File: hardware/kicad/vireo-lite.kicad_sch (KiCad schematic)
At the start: 0 parts

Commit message: usb interface
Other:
- removed sheet Analog Front End (AFE)
- sheet Inputs ports: added PHANTOM_48V; removed none
- sheet USB Interface ports: added USB_N, USB_P, VBUS_RAW; removed none
- sheet User Interface ports: added HIZ_FET_GATE; removed none

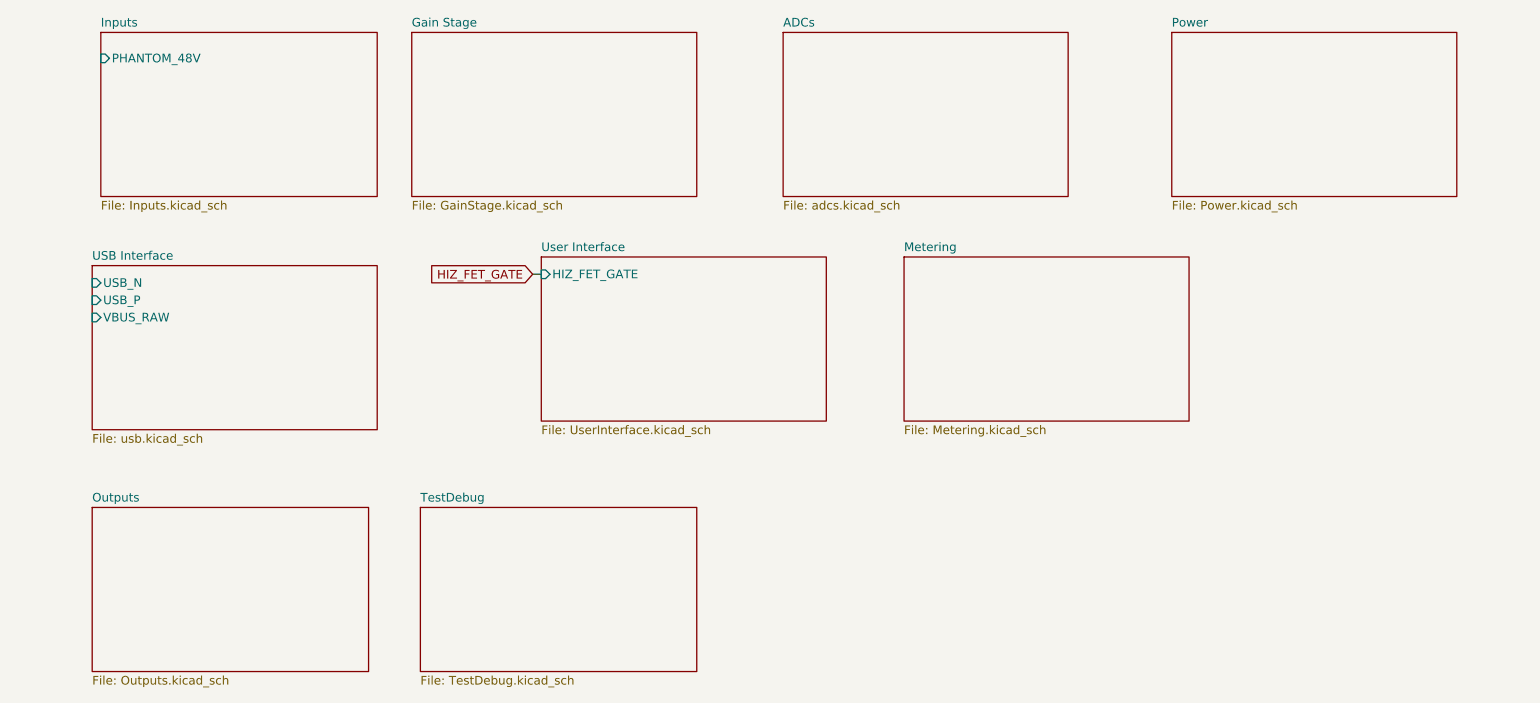
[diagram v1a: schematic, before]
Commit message: add phtm indicator and mcu sheet
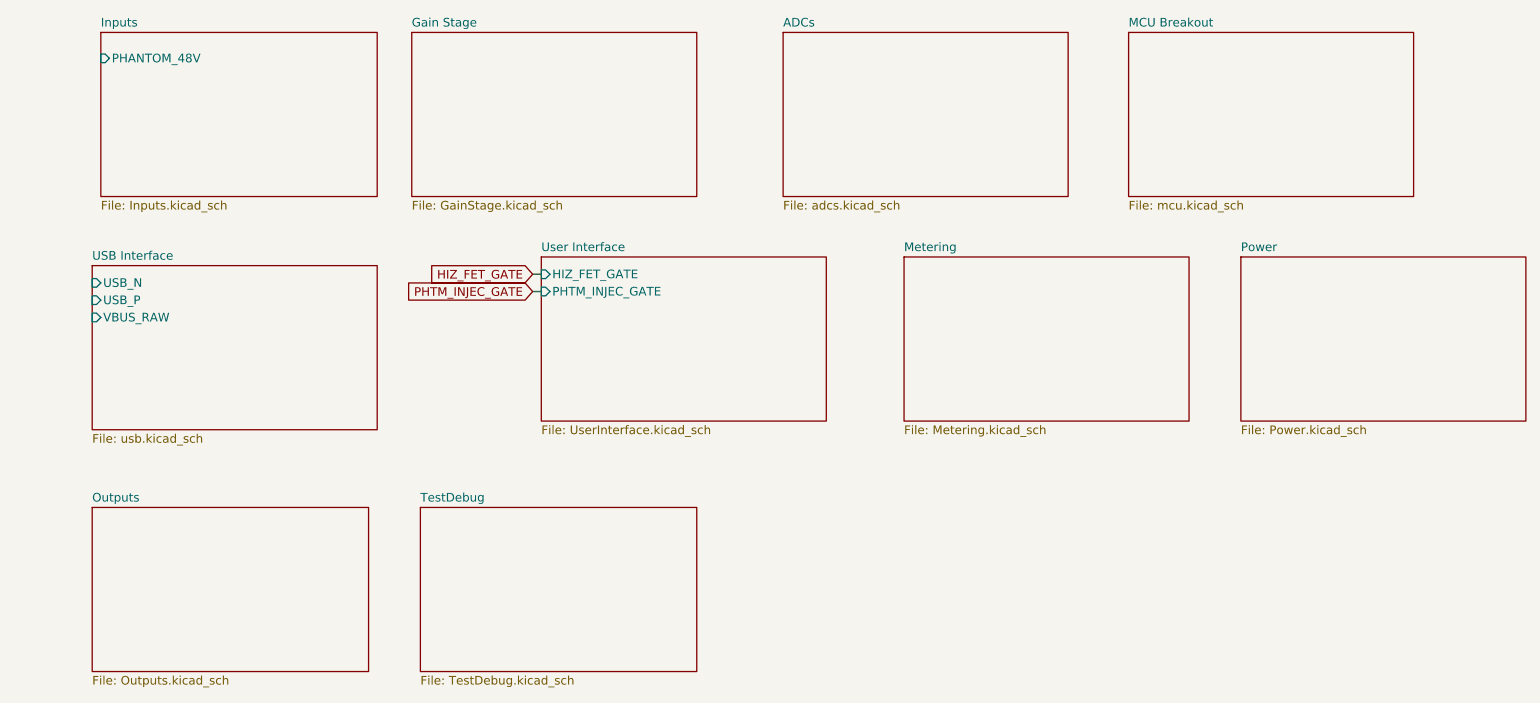
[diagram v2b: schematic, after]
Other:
- added sheet MCU Breakout (mcu.kicad_sch)
- sheet User Interface ports: added PHTM_INJEC_GATE; removed none
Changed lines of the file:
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@@
+		)
+	)
+	(wire
+		(pts
+			(xy 105.41 88.9) (xy 106.68 88.9)
+		)
+		(stroke
+			(width 0)
+			(type default)
 		)
 	)
@@
 		)
 	)
+	(global_label "PHTM_INJEC_GATE"
+		(shape input)
+		(at 105.41 88.9 180)
+		(fields_autoplaced yes)
+		(effects
+			(font
+				(size 1.27 1.27)
+			)
+			(justify right)
+		)
+		(property "Intersheetrefs" "${INTERSHEET_REFS}"
+			(at 85.673 88.9 0)
+			(hide yes)
+			(show_name no)
+			(do_not_autoplace no)
+			(effects
+				(font
+					(size 1.27 1.27)
+				)
+				(justify right)
+			)
+		)
+	)
 	(sheet
 		(at 87.63 50.8)
@@
 	)
 	(sheet
-		(at 199.39 50.8)
+		(at 209.55 83.82)
 		(size 41.91 24.13)
 		(exclude_from_sim no)
@@
 		)
 		(property "Sheetname" "Power"
-			(at 199.39 50.0884 0)
+			(at 209.55 83.1084 0)
 			(show_name no)
 			(do_not_autoplace no)
@@
 		)
 		(property "Sheetfile" "Power.kicad_sch"
-			(at 199.39 75.5146 0)
+			(at 209.55 108.5346 0)
 			(show_name no)
 			(do_not_autoplace no)
@@
 			)
 		)
+		(pin "PHTM_INJEC_GATE" input
+			(at 106.68 88.9 180)
+			(effects
+				(font
+					(size 1.27 1.27)
+				)
+				(justify left)
+			)
+		)
 		(instances
 			(project "vireo-lite"
@@
 				)
 			)
+		)
+	)
+	(sheet
+		(at 193.04 50.8)
+		(size 41.91 24.13)
+		(exclude_from_sim no)
+		(in_bom yes)
+		(on_board yes)
+		(dnp no)
+		(fields_autoplaced yes)
+		(stroke
+			(width 0.1524)
+			(type solid)
+		)
+		(fill
+			(color 0 0 0 0)
+		)
+		(property "Sheetname" "MCU Breakout"
+			(at 193.04 50.0884 0)
+			(show_name no)
+			(do_not_autoplace no)
+			(effects
+				(font
+					(size 1.27 1.27)
+				)
+				(justify left bottom)
+			)
+		)
+		(property "Sheetfile" "mcu.kicad_sch"
+			(at 193.04 75.5146 0)
+			(show_name no)
+			(do_not_autoplace no)
+			(effects
+				(font
+					(size 1.27 1.27)
+				)
+				(justify left top)
+			)
+		)
+		(instances
+			(project "vireo-lite"
+				(path "/61005c45-a979-4676-8d6b-817cd7f4616a"
+					(page "2")
+				)
+			)

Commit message: stm32h723 breakout
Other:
- sheet USB Interface renamed Flash and Debug Interface
- sheet Flash and Debug Interface: file usb.kicad_sch -> flash-debug.kicad_sch
- sheet Flash and Debug Interface ports: added SWDCLK, SWDIO; removed VBUS_RAW
- sheet MCU Breakout ports: added SWDCLK, SWDIO, USB_N, USB_P; removed none
